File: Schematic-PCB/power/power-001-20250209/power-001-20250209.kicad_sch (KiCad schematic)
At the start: 14 parts, among them J1 VIN, J2 Conn_01x02_Pin, J3 Conn_01x03_Pin, SW1 Locker, U1 PIC12F683-xSN, U2 LM1117MP-3.3

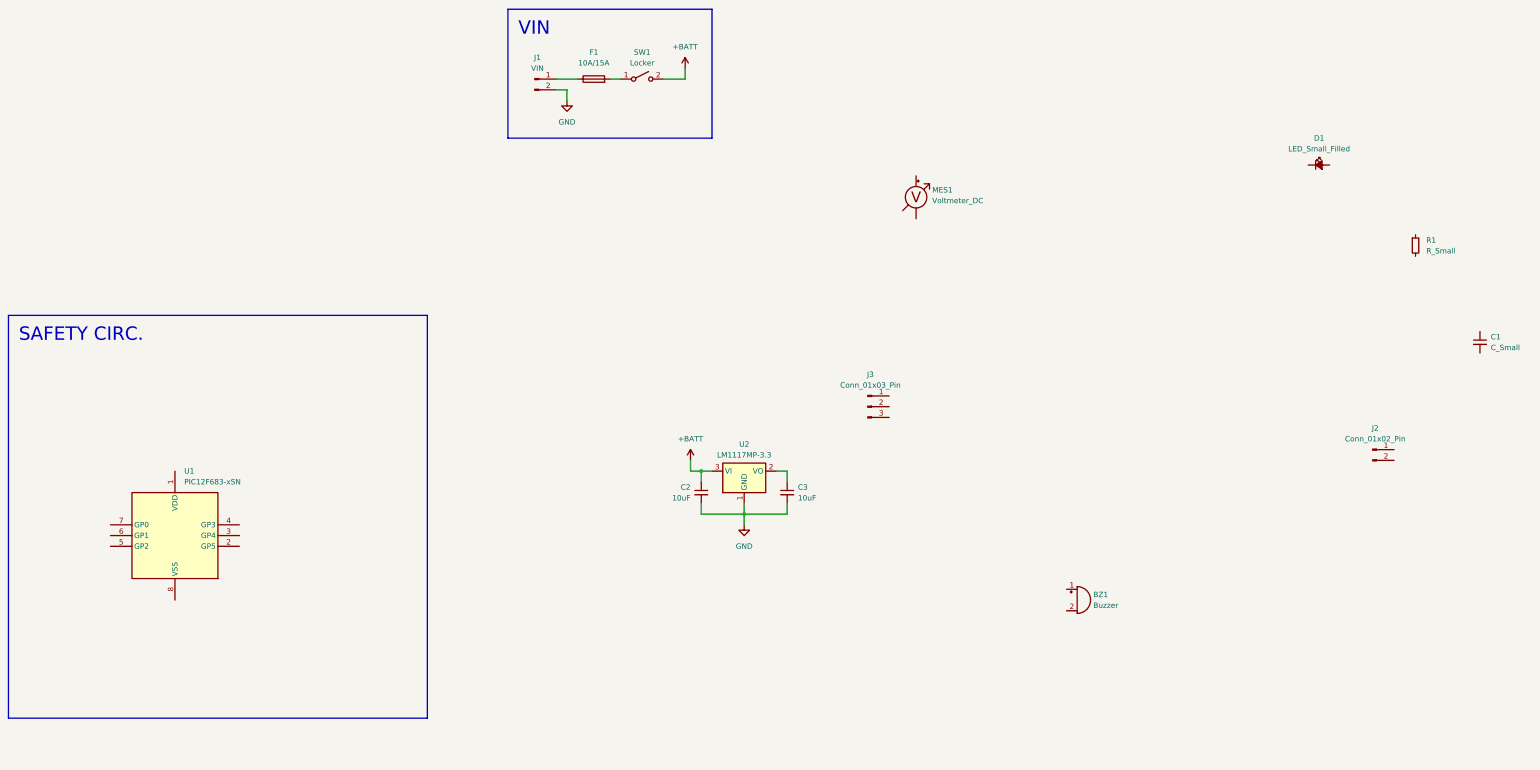
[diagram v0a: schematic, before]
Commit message: update: 電源基板 ver.001 の回路図を完成させた
DRが必要、ChatGPTを頼ってみる
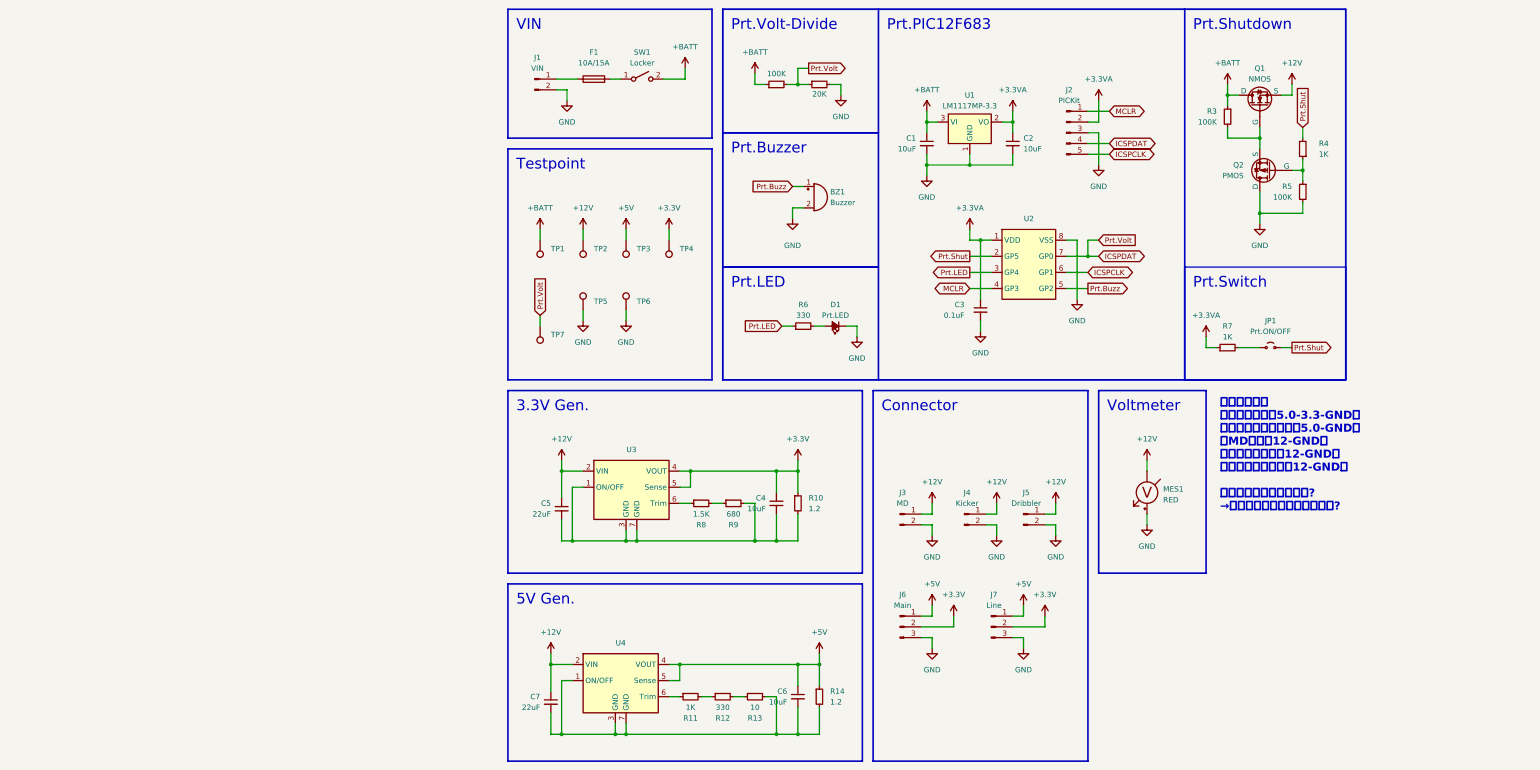
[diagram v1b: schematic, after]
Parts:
- removed U1: PIC12F683-xSN, Package_SO:SOIC-8_3.9x4.9mm_P1.27mm, symbol MCU_Microchip_PIC12:PIC12F683-xSN
- added C3: 0.1uF, symbol Device:C_Small
- added C4, C6: 10uF, symbol Device:C_Small
- added C7: 22uF, symbol Device:C_Small
- added J2: PICKit, symbol Connector:Conn_01x05_Pin
- added J4: Kicker, symbol Connector:Conn_01x02_Pin
- added J5: Dribbler, symbol Connector:Conn_01x02_Pin
- added J7: Line, symbol Connector:Conn_01x03_Pin
- added JP1: Prt.ON/OFF, symbol Jumper:Jumper_2_Small_Open
- added Q1: NMOS, symbol Simulation_SPICE:NMOS
- added Q2: PMOS, symbol Simulation_SPICE:PMOS
- added R10, R14: 1.2, symbol Device:R_Small
- added R11, R4, R7: 1K, symbol Device:R_Small
- added R12, R6: 330, symbol Device:R_Small
- added R13: 10, symbol Device:R_Small
- added R2: 20K, symbol Device:R_Small
- added R3, R5: 100K, symbol Device:R_Small
- added R8: 1.5K, symbol Device:R_Small
- added R9: 680, symbol Device:R_Small
- added TP1, TP2, TP3, TP4, TP5, TP6, TP7: TestPoint, symbol Connector:TestPoint
- added U2: ~, symbol @2025-power:PIC12F683
- added U3, U4: ~, symbol @2025-power:OKL-T6-W12N
- C5: renamed from C1; value C_Small -> 22uF
- D1: value LED_Small_Filled -> Prt.LED
- J3: renamed from J2; value Conn_01x02_Pin -> MD
- J6: renamed from J3; value Conn_01x03_Pin -> Main
- MES1: value Voltmeter_DC -> RED
- R1: value R_Small -> 100K
- renumbered C2 to C1, C3 to C2, U2 to U1
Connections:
- net +BATT: now also R1.1, Q1.1 (D), R3.1, TP1.1
- net GND: now also BZ1.2 (-), D1.1 (K), J3.2 (Pin_2), J6.3 (Pin_3), MES1.2 (+), C3.2, J2.3 (Pin_3), J4.2 (Pin_2), J5.2 (Pin_2), J7.3 (Pin_3), Q2.1 (D), R2.2, R5.2, TP5.1, TP6.1, U2.8 (VSS)
- net +3.3VA: now reaches C2.1, U1.2 (VO)
- net +3.3VA: now also C3.1, J2.2 (Pin_2), R7.1, U2.1 (VDD)
- net ICSPDAT: now reaches R1.2
- net ICSPDAT: now also J2.4 (Pin_4), R2.1, TP7.1, U2.7 (GP0)
- net +12V: now reaches MES1.1 (-)
- net +12V: now also C5.1, J3.1 (Pin_1), C7.1, J4.1 (Pin_1), J5.1 (Pin_1), Q1.3 (S), TP2.1, U3.2 (VIN), U4.2 (VIN)
- net at C5.2: now also C4.2, R10.2, R9.2, U3.1 (ON/OFF), U3.3 (GND), U3.7 (GND)
- net at D1.2 (A): now also R6.2
- net +5V: now reaches J6.1 (Pin_1)
- net +5V: now also C6.1, J7.1 (Pin_1), R14.1, TP3.1, U4.4 (VOUT), U4.5 (Sense)
- net +3.3V: now reaches J6.2 (Pin_2)
- net +3.3V: now also C4.1, J7.2 (Pin_2), R10.1, TP4.1, U3.4 (VOUT), U3.5 (Sense)
- net Prt.Buzz: now reaches BZ1.1 (+)
- net Prt.Buzz: now also U2.5 (GP2)
- new net: R8.1, U3.6 (Trim)
- new net: R8.2, R9.1
- new net: R11.1, U4.6 (Trim)
- new net: R11.2, R12.1
- new net: R12.2, R13.1
- new net: C6.2, C7.2, R13.2, R14.2, U4.1 (ON/OFF), U4.3 (GND), U4.7 (GND)
- new net: Q2.2 (G), R4.1, R5.1
- new net: JP1.1 (A), R7.2
- new net: Q1.2 (G), Q2.3 (S), R3.2
- new net ICSPCLK: J2.5 (Pin_5), U2.6 (GP1)
- new net MCLR: J2.1 (Pin_1), U2.4 (GP3)
- new net Prt.LED: R6.1, U2.3 (GP4)
- new net Prt.Shut: JP1.2 (B), R4.2, U2.2 (GP5)
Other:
- note added: "Div.Volt"
- note added: "【コネクタ】 ・メイン基板（5.0-3.3-GND） ・ラインセンサ基板（5.0-GND） ・MD基板（12-GND） ・キッカー基板（12-GND） ・ドリブラー基板（12-GND） 集約したほうがいいのか? →電圧降下はどのぐらい起きる?"
- moved on the sheet: BZ1, C1, C2, C5, J3, J6, MES1, U1

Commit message: add: MD基板 ver.001 のプロジェクトを作成した
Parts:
- added J4, J5: MD, symbol Connector:Conn_01x02_Pin
- renumbered J4 to J6, J5 to J7, J6 to J8, J7 to J9
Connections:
- net +12V: now also J4.1 (Pin_1), J5.1 (Pin_1)
- net GND: now also J4.2 (Pin_2), J5.2 (Pin_2)
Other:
- moved on the sheet: J3, J6, J7, J8, J9

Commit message: いろいろ追加した
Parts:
- BZ1, C1, C2, C3, C4, C5, C6, C7: footprint (none) -> Capacitor_SMD:C_0603_1608Metric
- F1: footprint (none) -> @2024-Power:Fuse
- J1: footprint (none) -> @2024-Power:VIN
- R1, R10, R11, R12, R13, R2, R3, R4, R5, R6, R7, R8, R9: footprint (none) -> Resistor_SMD:R_0603_1608Metric
- R14: value 1.2 -> 1.2K; footprint (none) -> Resistor_SMD:R_0603_1608Metric
- SW1: footprint (none) -> @2024-Power:RA1113112R
- TP1, TP2, TP3, TP4, TP5, TP6, TP7: footprint (none) -> TestPoint:TestPoint_Plated_Hole_D2.0mm
- U3, U4: footprint (none) -> @2024-Power:OKL-T6-W12N-C

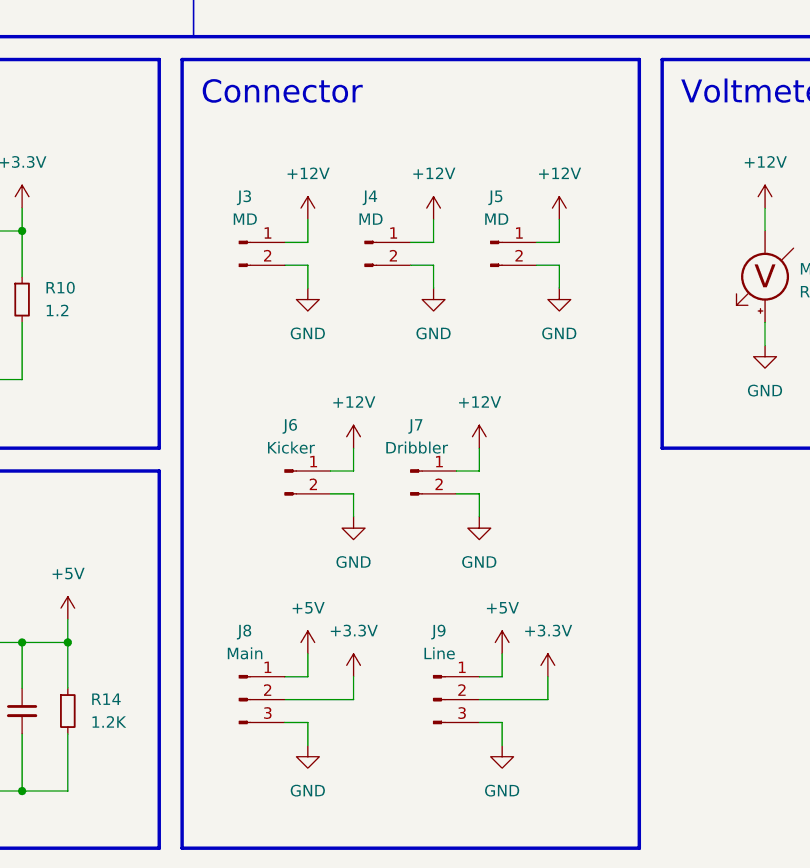
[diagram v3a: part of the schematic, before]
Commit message: update: 電源基板の回路図を開いた
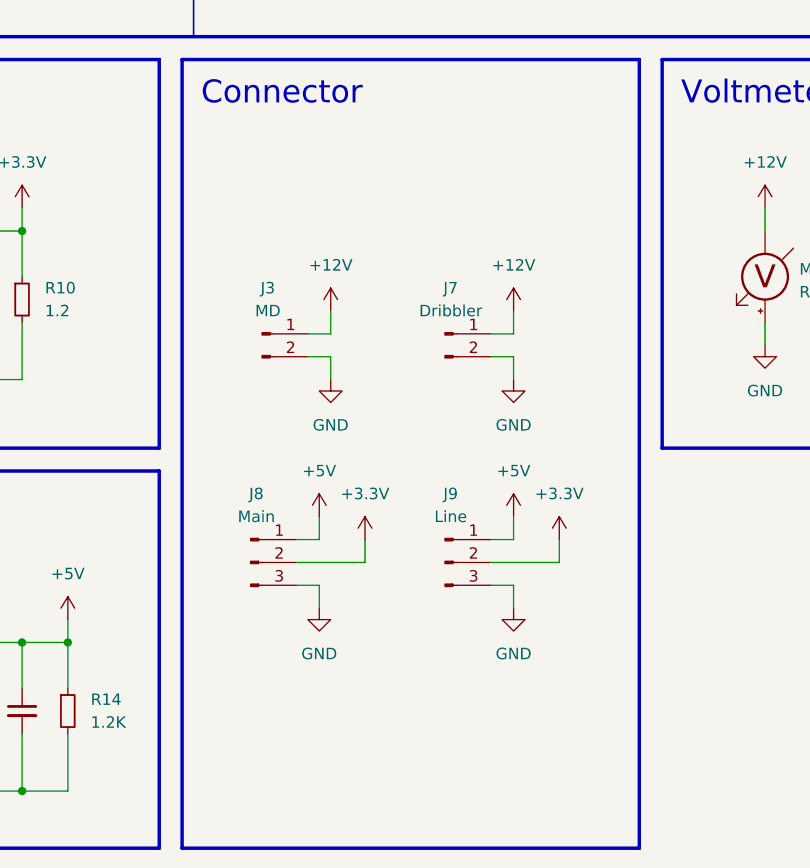
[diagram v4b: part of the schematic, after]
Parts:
- removed J4, J5: MD, symbol Connector:Conn_01x02_Pin
- removed J6: Kicker, symbol Connector:Conn_01x02_Pin
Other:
- moved on the sheet: J3, J7, J8, J9
